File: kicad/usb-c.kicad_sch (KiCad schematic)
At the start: 12 parts, among them J201 USB_C_Receptacle_USB2.0_16P, U201 TPD2S300

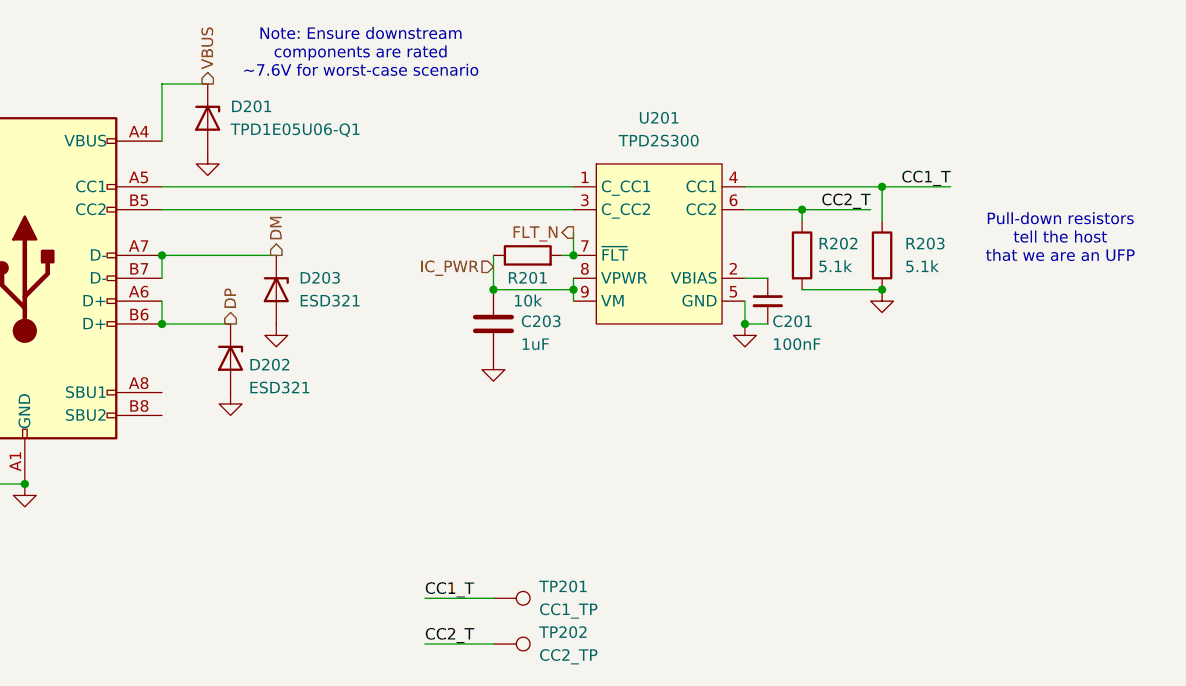
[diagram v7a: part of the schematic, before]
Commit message: refactor usb-c module, remove unnecessary ICs
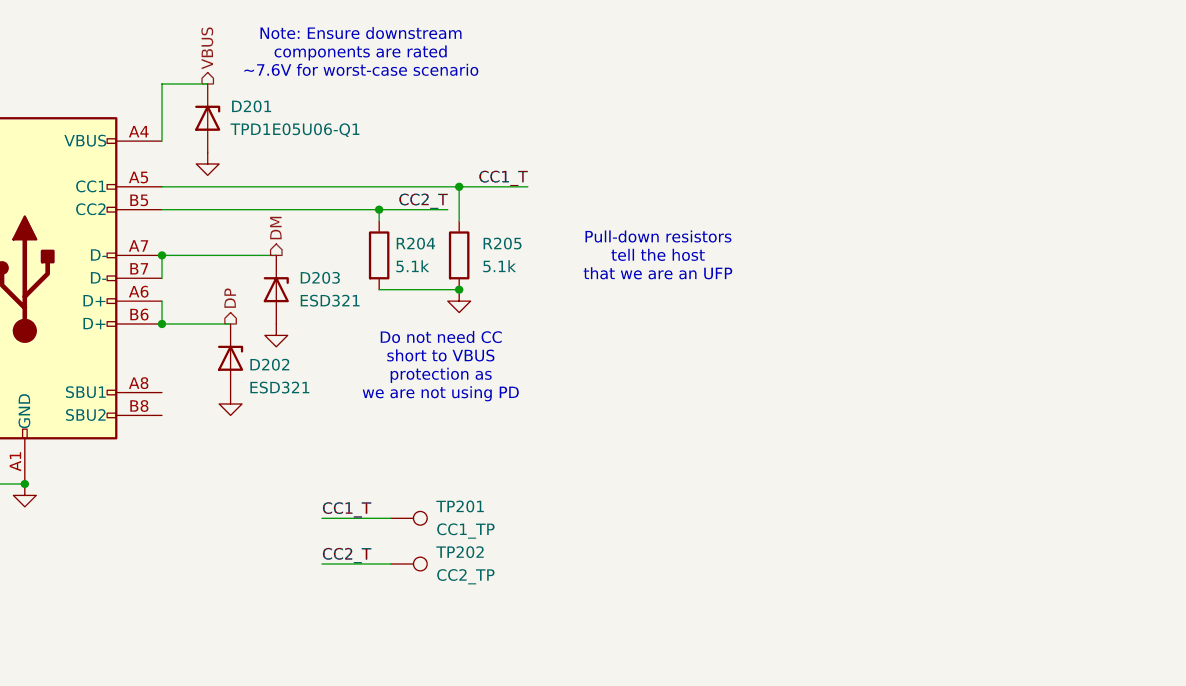
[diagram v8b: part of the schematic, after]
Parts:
- removed C201: 100nF, Capacitor_SMD:C_0603_1608Metric_Pad1.08x0.95mm_HandSolder, symbol Device:C_Small
- removed C203: 1uF, Capacitor_SMD:C_0805_2012Metric_Pad1.18x1.45mm_HandSolder, symbol Device:C
- removed R201: 10k, Resistor_SMD:R_0603_1608Metric_Pad0.98x0.95mm_HandSolder, symbol Device:R
- removed R202, R203: 5.1k, Resistor_SMD:R_0603_1608Metric_Pad0.98x0.95mm_HandSolder, symbol Device:R
- removed U201: TPD2S300, Raven:YFF0009AJAJ, symbol Raven:TPD2S300
- added R204, R205: 5.1k, Resistor_SMD:R_0603_1608Metric_Pad0.98x0.95mm_HandSolder, symbol Device:R
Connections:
- net CC1_T: now also J201.A5 (CC1), R205.1
- net CC2_T: now also J201.B5 (CC2), R204.1
- net GND: now also R204.2, R205.2
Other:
- note added: "Do not need CC short to VBUS protection as we are not using PD"
- moved on the sheet: TP201, TP202
